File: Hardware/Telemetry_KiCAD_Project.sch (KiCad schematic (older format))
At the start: 1 part, among them J1 50Ω SMA Connector

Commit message: Added test points to main schematic page
Also corrected library table
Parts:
- added TP? (x26): TestPoint_Small, symbol Connector:TestPoint_Small
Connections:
- wire segments 45 -> 71
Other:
- moved on the sheet: J1

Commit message: Added and connected test points
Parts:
- removed TP?: TestPoint_Small, symbol Connector:TestPoint_Small
- TP1, TP10, TP11, TP12, TP13, TP14, TP15, TP16, TP17, TP18, TP19, TP2, TP20, TP21, TP22, TP23, TP24, TP25, TP3, TP4, TP5, TP6, TP7, TP8, TP9: renamed from TP?; footprint (none) -> TestPoint:TestPoint_Loop_D1.80mm_Drill1.0mm_Beaded
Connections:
- wire segments 71 -> 70

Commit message: Added SPI debug connectors to SPI busses
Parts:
- removed TP1, TP10, TP11, TP12, TP13, TP14, TP15, TP16, TP17, TP18, TP19, TP2, TP20, TP21, TP22, TP23, TP24, TP25, TP3, TP4, TP5, TP6, TP7, TP8, TP9: TestPoint_Small, TestPoint:TestPoint_Loop_D1.80mm_Drill1.0mm_Beaded, symbol Connector:TestPoint_Small
- added J?: TX SPI Debug, symbol Connector_Generic:Conn_02x03_Odd_Even
- added J?: RX SPI Debug, symbol Connector_Generic:Conn_02x03_Odd_Even
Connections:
- wire segments 70 -> 55

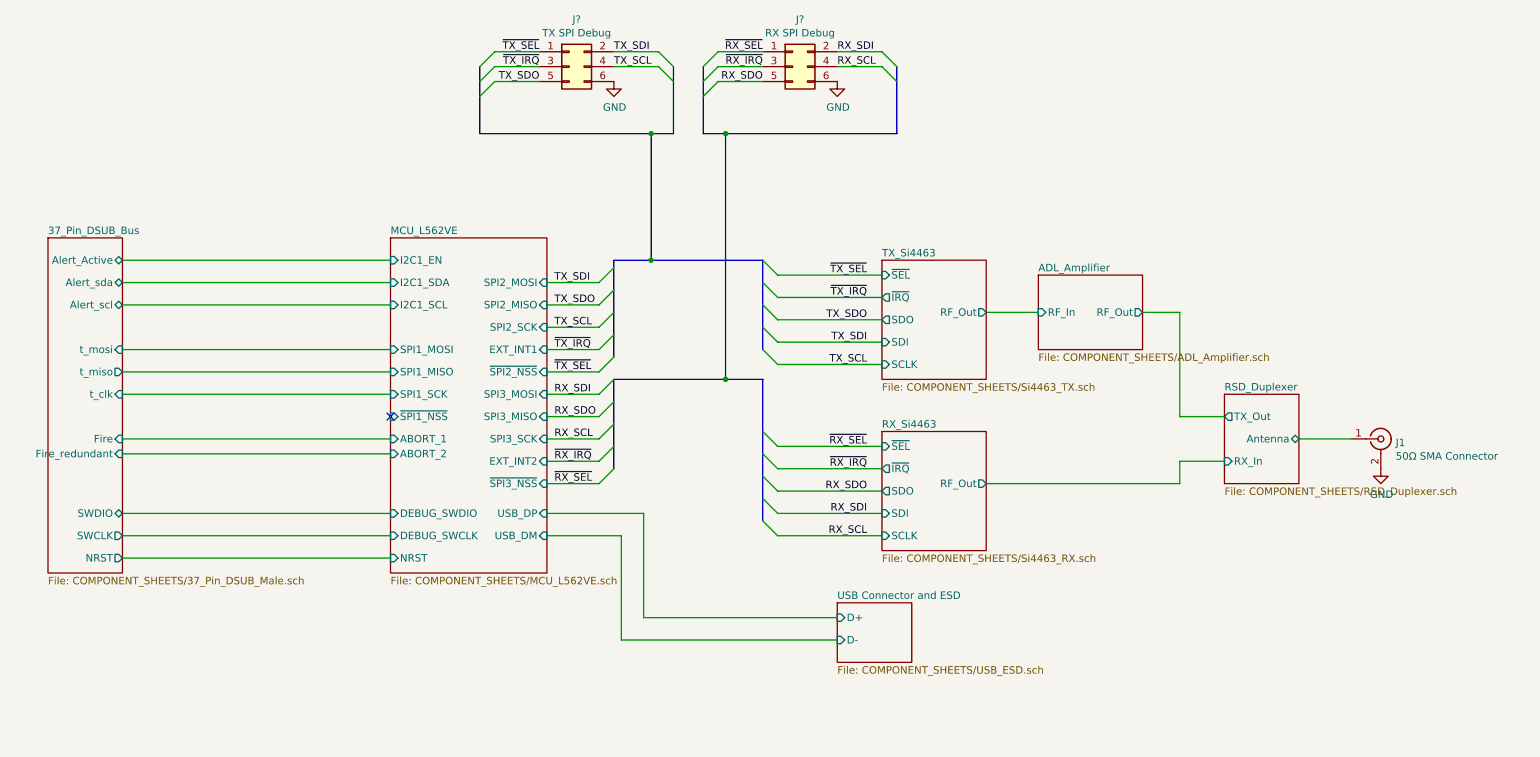
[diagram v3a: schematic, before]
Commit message: Arranged TX and RX chip matching networks
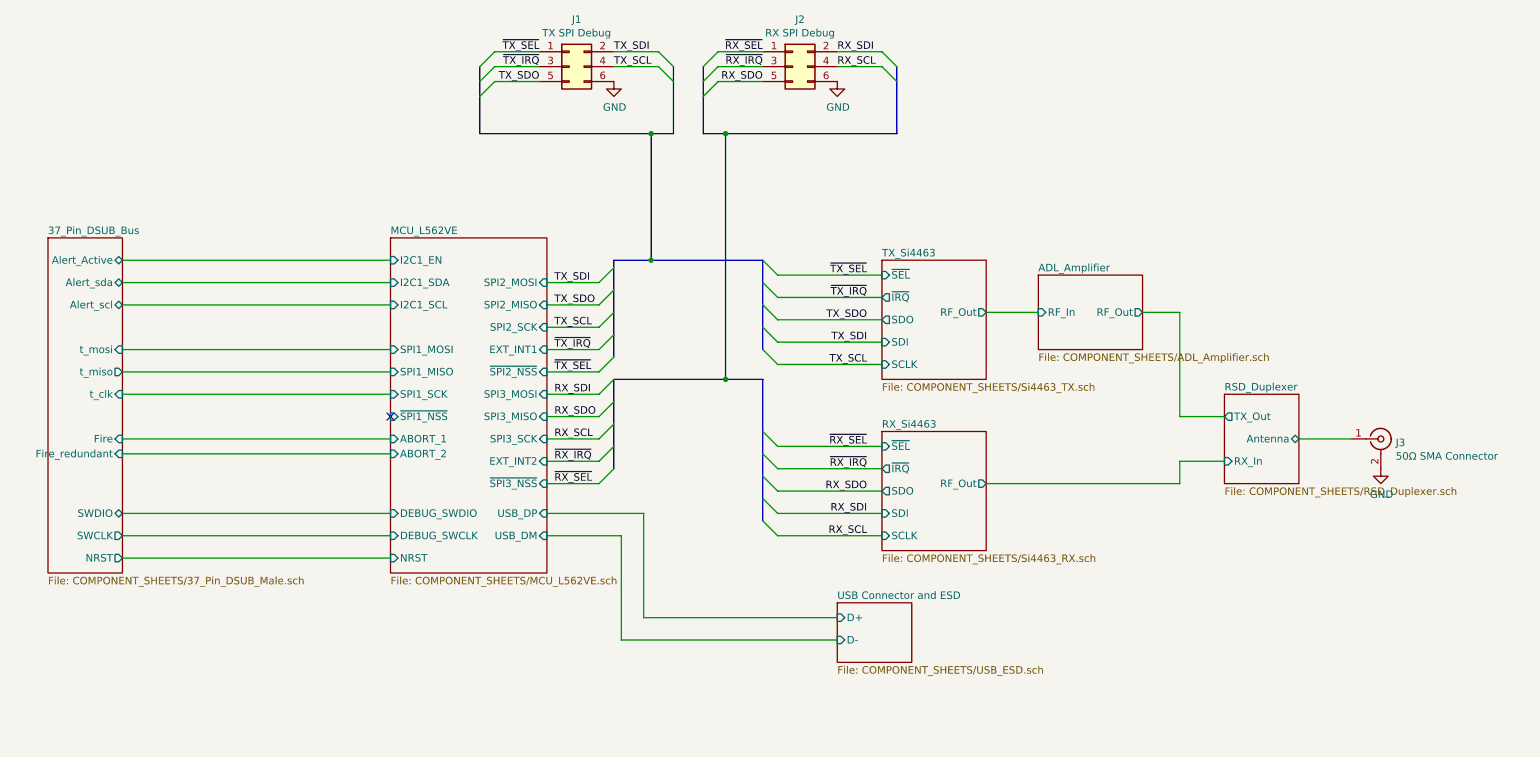
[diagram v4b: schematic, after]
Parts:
- J1, J2: renamed from J?; footprint (none) -> Connector_PinHeader_2.54mm:PinHeader_2x05_P2.54mm_Vertical
- renumbered J1 to J3
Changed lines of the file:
@@
 $EndDescr
 $Comp
-L Connector:Conn_Coaxial J1
+L Connector:Conn_Coaxial J3
 U 1 1 619FD788
 P 9700 3450
-F 0 "J1" H 9800 3425 50  0000 L CNN
+F 0 "J3" H 9800 3425 50  0000 L CNN
 F 1 "50Ω SMA Connector" H 9800 3334 50  0000 L CNN
 F 2 "Connector_Coaxial:SMA_Amphenol_132134-11_Vertical" H 9700 3450 50  0001 C CNN
@@
 $EndComp
 $Comp
-L power:GND #PWR0101
+L power:GND #PWR03
 U 1 1 619FE4AD
 P 9700 3650
-F 0 "#PWR0101" H 9700 3400 50  0001 C CNN
+F 0 "#PWR03" H 9700 3400 50  0001 C CNN
 F 1 "GND" H 9705 3477 50  0000 C CNN
 F 2 "" H 9700 3650 50  0001 C CNN
@@
 	7050 3750 8350 3750
 $Comp
-L Connector_Generic:Conn_02x03_Odd_Even J?
+L Connector_Generic:Conn_02x03_Odd_Even J1
 U 1 1 61BF0412
 P 4250 950
-F 0 "J?" H 4300 1267 50  0000 C CNN
+F 0 "J1" H 4300 1267 50  0000 C CNN
 F 1 "TX SPI Debug" H 4300 1176 50  0000 C CNN
-F 2 "" H 4250 950 50  0001 C CNN
+F 2 "Connector_PinHeader_2.54mm:PinHeader_2x05_P2.54mm_Vertical" H 4250 950 50  0001 C CNN
 F 3 "~" H 4250 950 50  0001 C CNN
 	1    4250 950
@@
 $EndComp
 $Comp
-L Connector_Generic:Conn_02x03_Odd_Even J?
+L Connector_Generic:Conn_02x03_Odd_Even J2
 U 1 1 61BF15AF
 P 5750 950
-F 0 "J?" H 5800 1267 50  0000 C CNN
+F 0 "J2" H 5800 1267 50  0000 C CNN
 F 1 "RX SPI Debug" H 5800 1176 50  0000 C CNN
-F 2 "" H 5750 950 50  0001 C CNN
+F 2 "Connector_PinHeader_2.54mm:PinHeader_2x05_P2.54mm_Vertical" H 5750 950 50  0001 C CNN
 F 3 "~" H 5750 950 50  0001 C CNN
 	1    5750 950
@@
 TX_SCL
 $Comp
-L power:GND #PWR?
+L power:GND #PWR01
 U 1 1 61BF6E76
 P 4550 1050
-F 0 "#PWR?" H 4550 800 50  0001 C CNN
+F 0 "#PWR01" H 4550 800 50  0001 C CNN
 F 1 "GND" H 4555 877 50  0000 C CNN
 F 2 "" H 4550 1050 50  0001 C CNN
@@
 RX_SCL
 $Comp
-L power:GND #PWR?
+L power:GND #PWR02
 U 1 1 61BF7DA6
 P 6050 1050
-F 0 "#PWR?" H 6050 800 50  0001 C CNN
+F 0 "#PWR02" H 6050 800 50  0001 C CNN
 F 1 "GND" H 6055 877 50  0000 C CNN
 F 2 "" H 6050 1050 50  0001 C CNN

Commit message: Adjustments to RF chip placements
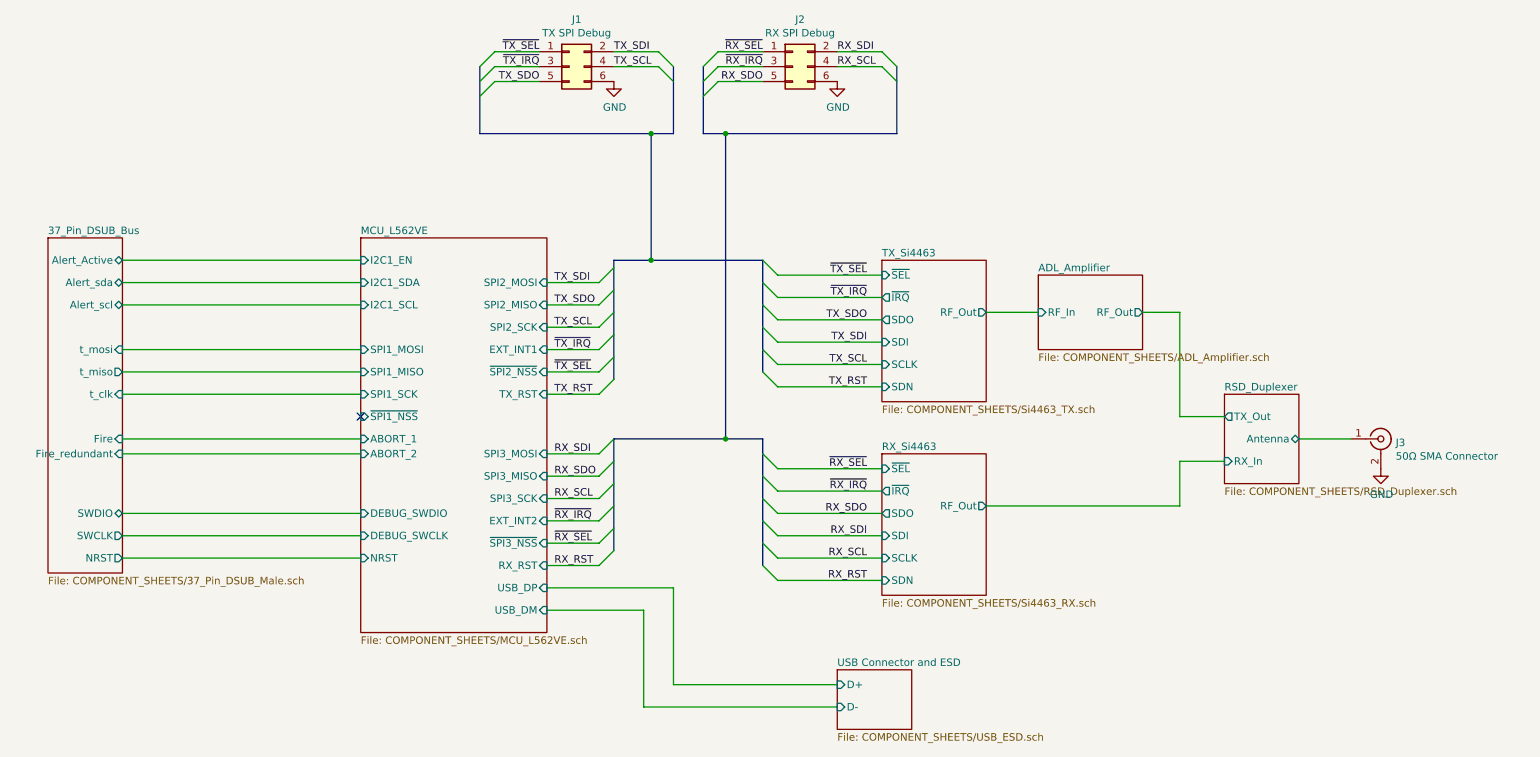
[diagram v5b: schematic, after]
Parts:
- J1, J2: footprint Connector_PinHeader_2.54mm:PinHeader_2x05_P2.54mm_Vertical -> Connector_PinHeader_2.54mm:PinHeader_2x03_P2.54mm_Vertical
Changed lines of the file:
@@
 	8650 3600 8350 3600
 Wire Wire Line
-	8350 3600 8350 3750
+	8350 3600 8350 3900
 Text Label 6250 2650 2    50   ~ 0
 TX_SDO
@@
 Text Label 6250 2950 2    50   ~ 0
 TX_SCL
-Text Label 6250 3800 2    50   ~ 0
+Text Label 6250 3950 2    50   ~ 0
 RX_SDO
-Text Label 6250 3950 2    50   ~ 0
+Text Label 6250 4100 2    50   ~ 0
 RX_SDI
-Text Label 6250 4100 2    50   ~ 0
+Text Label 6250 4250 2    50   ~ 0
 RX_SCL
 Entry Wire Line
@@
 Text Label 4150 2700 0    50   ~ 0
 TX_SCL
-Text Label 4150 3300 0    50   ~ 0
+Text Label 4150 3700 0    50   ~ 0
 RX_SDO
-Text Label 4150 3150 0    50   ~ 0
+Text Label 4150 3550 0    50   ~ 0
 RX_SDI
-Text Label 4150 3450 0    50   ~ 0
+Text Label 4150 3850 0    50   ~ 0
 RX_SCL
 Entry Wire Line
@@
 	4450 2700 4550 2600
 Entry Wire Line
-	4450 3150 4550 3050
-Entry Wire Line
-	4450 3300 4550 3200
-Entry Wire Line
-	4450 3450 4550 3350
+	4450 3550 4550 3450
+Entry Wire Line
+	4450 3700 4550 3600
+Entry Wire Line
+	4450 3850 4550 3750
 Wire Wire Line
 	4450 2400 4100 2400
@@
 	4450 2700 4100 2700
 Wire Wire Line
-	4100 3150 4450 3150
-Wire Wire Line
-	4450 3300 4100 3300
-Wire Wire Line
-	4100 3450 4450 3450
-Wire Wire Line
-	4750 4650 4750 3950
-Wire Wire Line
-	4750 3950 4100 3950
-Wire Wire Line
-	4100 4100 4600 4100
-Wire Wire Line
-	4600 4100 4600 4800
+	4100 3550 4450 3550
+Wire Wire Line
+	4450 3700 4100 3700
+Wire Wire Line
+	4100 3850 4450 3850
 Entry Wire Line
 	4450 2850 4550 2750
 Entry Wire Line
-	4450 3600 4550 3500
-Wire Wire Line
-	4450 3600 4100 3600
+	4450 4000 4550 3900
+Wire Wire Line
+	4450 4000 4100 4000
 Wire Wire Line
 	4100 2850 4450 2850
 Text Label 4150 2850 0    50   ~ 0
 ~TX_IRQ
-Text Label 4150 3600 0    50   ~ 0
+Text Label 4150 4000 0    50   ~ 0
 ~RX_IRQ
 Entry Wire Line
@@
 Text Label 6250 2500 2    50   ~ 0
 ~TX_IRQ
-Text Label 6250 3650 2    50   ~ 0
+Text Label 6250 3800 2    50   ~ 0
 ~RX_IRQ
 Entry Wire Line
-	4450 3750 4550 3650
+	4450 4150 4550 4050
 Entry Wire Line
 	4450 3000 4550 2900
@@
 	4100 3000 4450 3000
 Wire Wire Line
-	4100 3750 4450 3750
+	4100 4150 4450 4150
 Text Label 4150 3000 0    50   ~ 0
 ~TX_SEL
 Entry Wire Line
 	5550 2250 5650 2350
-Text Label 4150 3750 0    50   ~ 0
+Text Label 4150 4150 0    50   ~ 0
 ~RX_SEL
 Text Label 6250 2350 2    50   ~ 0
 ~TX_SEL
-Entry Wire Line
-	5550 3400 5650 3500
-Text Label 6250 3500 2    50   ~ 0
+Text Label 6250 3650 2    50   ~ 0
 ~RX_SEL
-NoConn ~ 3050 3300
-$Sheet
-S 3050 2100 1050 2250
-U 61A107A5
-F0 "MCU_L562VE" 50
-F1 "COMPONENT_SHEETS/MCU_L562VE.sch" 50
-F2 "I2C1_SCL" I L 3050 2550 50
-F3 "I2C1_SDA" I L 3050 2400 50
-F4 "I2C1_EN" I L 3050 2250 50
-F5 "DEBUG_SWCLK" I L 3050 4100 50
-F6 "~SPI2_NSS" I R 4100 3000 50
-F7 "SPI3_MOSI" I R 4100 3150 50
-F8 "SPI3_MISO" I R 4100 3300 50
-F9 "SPI3_SCK" I R 4100 3450 50
-F10 "DEBUG_SWDIO" I L 3050 3950 50
-F11 "USB_DP" I R 4100 3950 50
-F12 "USB_DM" I R 4100 4100 50
-F13 "SPI2_SCK" I R 4100 2700 50
-F14 "SPI2_MISO" I R 4100 2550 50
-F15 "SPI2_MOSI" I R 4100 2400 50
-F16 "~SPI3_NSS" I R 4100 3750 50
-F17 "SPI1_SCK" I L 3050 3150 50
-F18 "SPI1_MISO" I L 3050 3000 50
-F19 "SPI1_MOSI" I L 3050 2850 50
-F20 "~SPI1_NSS" I L 3050 3300 50
-F21 "EXT_INT1" I R 4100 2850 50
-F22 "NRST" I L 3050 4250 50
-F23 "ABORT_1" I L 3050 3450 50
-F24 "ABORT_2" I L 3050 3550 50
-F25 "EXT_INT2" I R 4100 3600 50
-$EndSheet
-$Sheet
-S 6350 2250 700  800
-U 619D9C89
-F0 "TX_Si4463" 50
-F1 "COMPONENT_SHEETS/Si4463_TX.sch" 50
-F2 "~SEL" I L 6350 2350 50
-F3 "SDI" I L 6350 2800 50
-F4 "SCLK" I L 6350 2950 50
-F5 "~IRQ" O L 6350 2500 50
-F6 "SDO" O L 6350 2650 50
-F7 "RF_Out" O R 7050 2600 50
-$EndSheet
-$Sheet
-S 6350 3400 700  800
+$Sheet
+S 6350 3550 700  950
 U 61A0416A
 F0 "RX_Si4463" 50
 F1 "COMPONENT_SHEETS/Si4463_RX.sch" 50
-F2 "~SEL" I L 6350 3500 50
-F3 "SDI" I L 6350 3950 50
-F4 "SCLK" I L 6350 4100 50
-F5 "~IRQ" O L 6350 3650 50
-F6 "SDO" O L 6350 3800 50
-F7 "RF_Out" O R 7050 3750 50
+F2 "~SEL" I L 6350 3650 50
+F3 "SDI" I L 6350 4100 50
+F4 "SCLK" I L 6350 4250 50
+F5 "~IRQ" O L 6350 3800 50
+F6 "SDO" O L 6350 3950 50
+F7 "RF_Out" O R 7050 3900 50
+F8 "SDN" I L 6350 4400 50
 $EndSheet
 $Sheet
@@
 $EndSheet
 $Sheet
-S 6050 4550 500  400
+S 6050 5000 500  400
 U 61A2ED84
 F0 "USB Connector and ESD" 50
 F1 "COMPONENT_SHEETS/USB_ESD.sch" 50
-F2 "D-" I L 6050 4800 50
-F3 "D+" I L 6050 4650 50
-$EndSheet
-$Sheet
-S 750  2100 500  2250
-U 619DC150
-F0 "37_Pin_DSUB_Bus" 50
-F1 "COMPONENT_SHEETS/37_Pin_DSUB_Male.sch" 50
-F2 "t_mosi" I R 1250 2850 50
-F3 "t_clk" I R 1250 3150 50
-F4 "Fire" I R 1250 3450 50
-F5 "Fire_redundant" I R 1250 3550 50
-F6 "Alert_Active" B R 1250 2250 50
-F7 "Alert_scl" B R 1250 2550 50
-F8 "Alert_sda" B R 1250 2400 50
-F9 "t_miso" O R 1250 3000 50
-F10 "SWDIO" B R 1250 3950 50
-F11 "SWCLK" O R 1250 4100 50
-F12 "NRST" O R 1250 4250 50
+F2 "D-" I L 6050 5250 50
+F3 "D+" I L 6050 5100 50
 $EndSheet
 Wire Wire Line
 	9150 3450 9500 3450
 Wire Wire Line
-	1250 2250 3050 2250
-Wire Wire Line
-	1250 2400 3050 2400
-Wire Wire Line
-	1250 2550 3050 2550
-Wire Wire Line
-	1250 2850 3050 2850
-Wire Wire Line
-	1250 3000 3050 3000
-Wire Wire Line
-	1250 3150 3050 3150
-Wire Wire Line
-	1250 3450 3050 3450
-Wire Wire Line
-	1250 3550 3050 3550
-Wire Wire Line
-	1250 3950 3050 3950
-Wire Wire Line
-	1250 4100 3050 4100
-Wire Wire Line
-	1250 4250 3050 4250
-Wire Wire Line
 	5650 2350 6350 2350
 Wire Wire Line
@@
 	5650 2950 6350 2950
 Wire Wire Line
-	5650 3500 6350 3500
-Wire Wire Line
 	5650 3650 6350 3650
 Wire Wire Line
@@
 	5650 4100 6350 4100
 Wire Wire Line
-	4750 4650 6050 4650
-Wire Wire Line
-	4600 4800 6050 4800
+	5650 4250 6350 4250
 Wire Wire Line
 	7050 2600 7400 2600
 Wire Wire Line
-	7050 3750 8350 3750
+	7050 3900 8350 3900
 $Comp
 L Connector_Generic:Conn_02x03_Odd_Even J1
@@
 F 0 "J1" H 4300 1267 50  0000 C CNN
 F 1 "TX SPI Debug" H 4300 1176 50  0000 C CNN
-F 2 "Connector_PinHeader_2.54mm:PinHeader_2x05_P2.54mm_Vertical" H 4250 950 50  0001 C CNN
+F 2 "Connector_PinHeader_2.54mm:PinHeader_2x03_P2.54mm_Vertical" H 4250 950 50  0001 C CNN
 F 3 "~" H 4250 950 50  0001 C CNN
 	1    4250 950
@@
 F 0 "J2" H 5800 1267 50  0000 C CNN
 F 1 "RX SPI Debug" H 5800 1176 50  0000 C CNN
-F 2 "Connector_PinHeader_2.54mm:PinHeader_2x05_P2.54mm_Vertical" H 5750 950 50  0001 C CNN
+F 2 "Connector_PinHeader_2.54mm:PinHeader_2x03_P2.54mm_Vertical" H 5750 950 50  0001 C CNN
 F 3 "~" H 5750 950 50  0001 C CNN
 	1    5750 950
@@
 Connection ~ 5300 1400
 Wire Bus Line
-	5300 1400 5300 3050
-Connection ~ 5300 3050
-Wire Bus Line
-	5300 3050 4550 3050
-Wire Bus Line
-	5300 3050 5550 3050
+	5300 1400 5300 3450
+Wire Bus Line
+	5300 3450 4550 3450
+Wire Bus Line
+	5300 3450 5550 3450
+$Sheet
+S 6350 2250 700  950
+U 619D9C89
+F0 "TX_Si4463" 50
+F1 "COMPONENT_SHEETS/Si4463_TX.sch" 50
+F2 "~SEL" I L 6350 2350 50
+F3 "SDI" I L 6350 2800 50
+F4 "SCLK" I L 6350 2950 50
+F5 "~IRQ" O L 6350 2500 50
+F6 "SDO" O L 6350 2650 50
+F7 "RF_Out" O R 7050 2600 50
+F8 "SDN" I L 6350 3100 50
+$EndSheet
+Wire Wire Line
+	4100 4450 4950 4450
+Wire Wire Line
+	4950 4450 4950 5100
+Wire Wire Line
+	4950 5100 6050 5100
+Wire Wire Line
+	6050 5250 4750 5250
+Wire Wire Line
+	4750 5250 4750 4600
+Wire Wire Line
+	4750 4600 4100 4600
+$Sheet
+S 750  2100 500  2250
+U 619DC150
+F0 "37_Pin_DSUB_Bus" 50
+F1 "COMPONENT_SHEETS/37_Pin_DSUB_Male.sch" 50
+F2 "t_mosi" I R 1250 2850 50
+F3 "t_clk" I R 1250 3150 50
+F4 "Fire" I R 1250 3450 50
+F5 "Fire_redundant" I R 1250 3550 50
+F6 "Alert_Active" B R 1250 2250 50
+F7 "Alert_scl" B R 1250 2550 50
+F8 "Alert_sda" B R 1250 2400 50
+F9 "t_miso" O R 1250 3000 50
+F10 "SWDIO" B R 1250 3950 50
+F11 "SWCLK" O R 1250 4100 50
+F12 "NRST" O R 1250 4250 50
+$EndSheet
+$Sheet
+S 2850 2100 1250 2650
+U 61A107A5
+F0 "MCU_L562VE" 50
+F1 "COMPONENT_SHEETS/MCU_L562VE.sch" 50
+F2 "I2C1_SCL" I L 2850 2550 50
+F3 "I2C1_SDA" I L 2850 2400 50
+F4 "I2C1_EN" I L 2850 2250 50
+F5 "DEBUG_SWCLK" I L 2850 4100 50
+F6 "~SPI2_NSS" I R 4100 3000 50
+F7 "SPI3_MOSI" I R 4100 3550 50
+F8 "SPI3_MISO" I R 4100 3700 50
+F9 "SPI3_SCK" I R 4100 3850 50
+F10 "DEBUG_SWDIO" I L 2850 3950 50
+F11 "USB_DP" I R 4100 4450 50
+F12 "USB_DM" I R 4100 4600 50
+F13 "SPI2_SCK" I R 4100 2700 50
+F14 "SPI2_MISO" I R 4100 2550 50
+F15 "SPI2_MOSI" I R 4100 2400 50
+F16 "~SPI3_NSS" I R 4100 4150 50
+F17 "SPI1_SCK" I L 2850 3150 50
+F18 "SPI1_MISO" I L 2850 3000 50
+F19 "SPI1_MOSI" I L 2850 2850 50
+F20 "~SPI1_NSS" I L 2850 3300 50
+F21 "EXT_INT1" I R 4100 2850 50
+F22 "NRST" I L 2850 4250 50
+F23 "ABORT_1" I L 2850 3450 50
+F24 "ABORT_2" I L 2850 3550 50
+F25 "EXT_INT2" I R 4100 4000 50
+F26 "RX_RST" I R 4100 4300 50
+F27 "TX_RST" I R 4100 3150 50
+$EndSheet
+Wire Wire Line
+	2850 2250 1250 2250
+Wire Wire Line
+	1250 2400 2850 2400
+Wire Wire Line
+	2850 2550 1250 2550
+Wire Wire Line
+	1250 2850 2850 2850
+Wire Wire Line
+	1250 3000 2850 3000
+Wire Wire Line
+	2850 3150 1250 3150
+Wire Wire Line
+	1250 3450 2850 3450
+Wire Wire Line
+	1250 3550 2850 3550
+Wire Wire Line
+	2850 3950 1250 3950
+Wire Wire Line
+	1250 4100 2850 4100
+Wire Wire Line
+	2850 4250 1250 4250
+NoConn ~ 2850 3300
+Connection ~ 5300 3450
+Entry Wire Line
+	5650 4250 5550 4150
+Entry Wire Line
+	5550 4300 5650 4400
+Wire Wire Line
+	5650 4400 6350 4400
+Entry Wire Line
+	4550 3050 4450 3150
+Entry Wire Line
+	4550 4200 4450 4300
+Wire Wire Line
+	4450 3150 4100 3150
+Wire Wire Line
+	4450 4300 4100 4300
+Text Label 4150 3150 0    50   ~ 0
+TX_RST
+Text Label 4150 4300 0    50   ~ 0
+RX_RST
+Entry Wire Line
+	5550 3000 5650 3100
+Wire Wire Line
+	5650 3100 6350 3100
+Text Label 6250 3100 2    50   ~ 0
+TX_RST
+Text Label 6250 4400 2    50   ~ 0
+RX_RST
 Wire Bus Line
 	6450 950  6450 1400
@@
 	3650 950  3650 1400
 Wire Bus Line
-	4550 3050 4550 3650
-Wire Bus Line
-	4550 2250 4550 2900
-Wire Bus Line
-	5550 2250 5550 2850
-Wire Bus Line
-	5550 3050 5550 4000
+	4550 3450 4550 4200
+Wire Bus Line
+	5550 3450 5550 4300
+Wire Bus Line
+	5550 2250 5550 3000
+Wire Bus Line
+	4550 2250 4550 3050
 $EndSCHEMATC
